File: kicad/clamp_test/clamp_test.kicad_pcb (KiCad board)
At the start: 2 copper layers, 48.3 x 29.2 mm, 22 parts, among them J1 Conn_Coaxial, J2 Conn_Coaxial, J3 Conn_01x03_Pin, U1 LT1365CS, U2 BUF634A

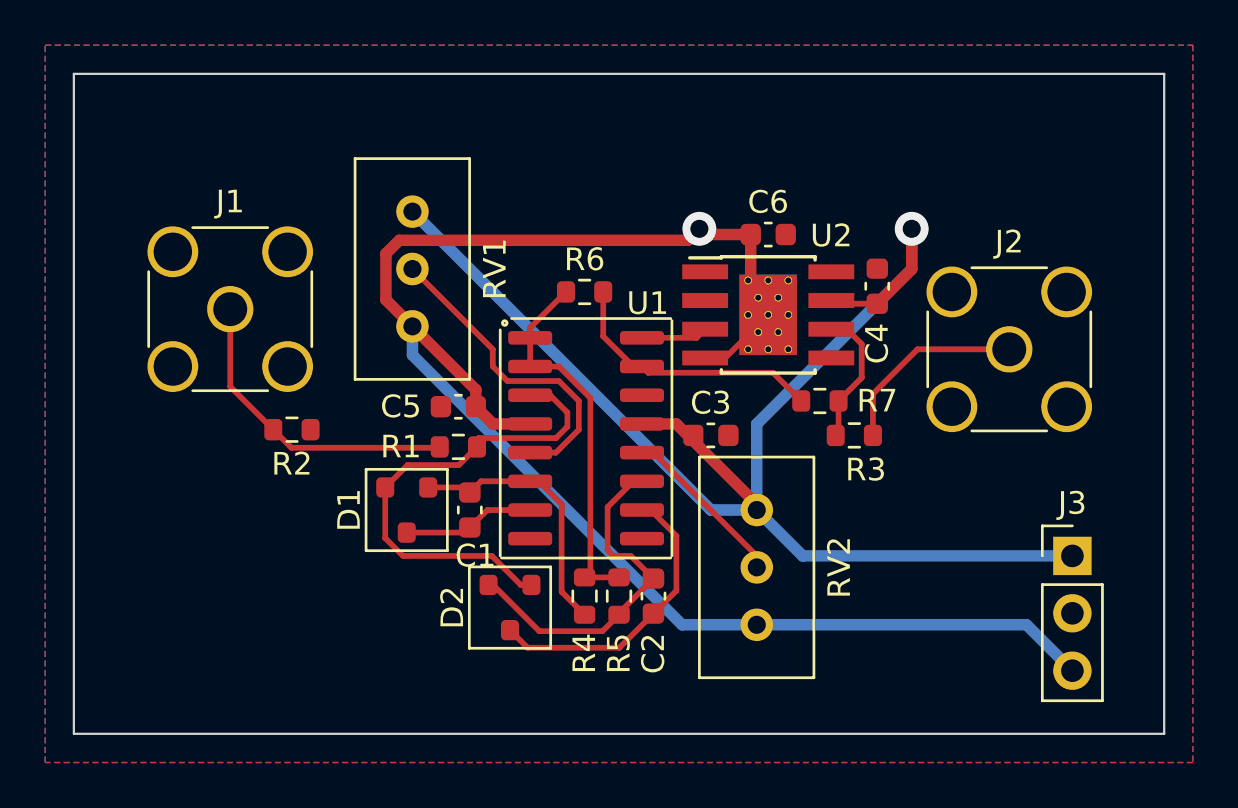
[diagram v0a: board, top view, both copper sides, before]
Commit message: Clamp test board: removed unused vias
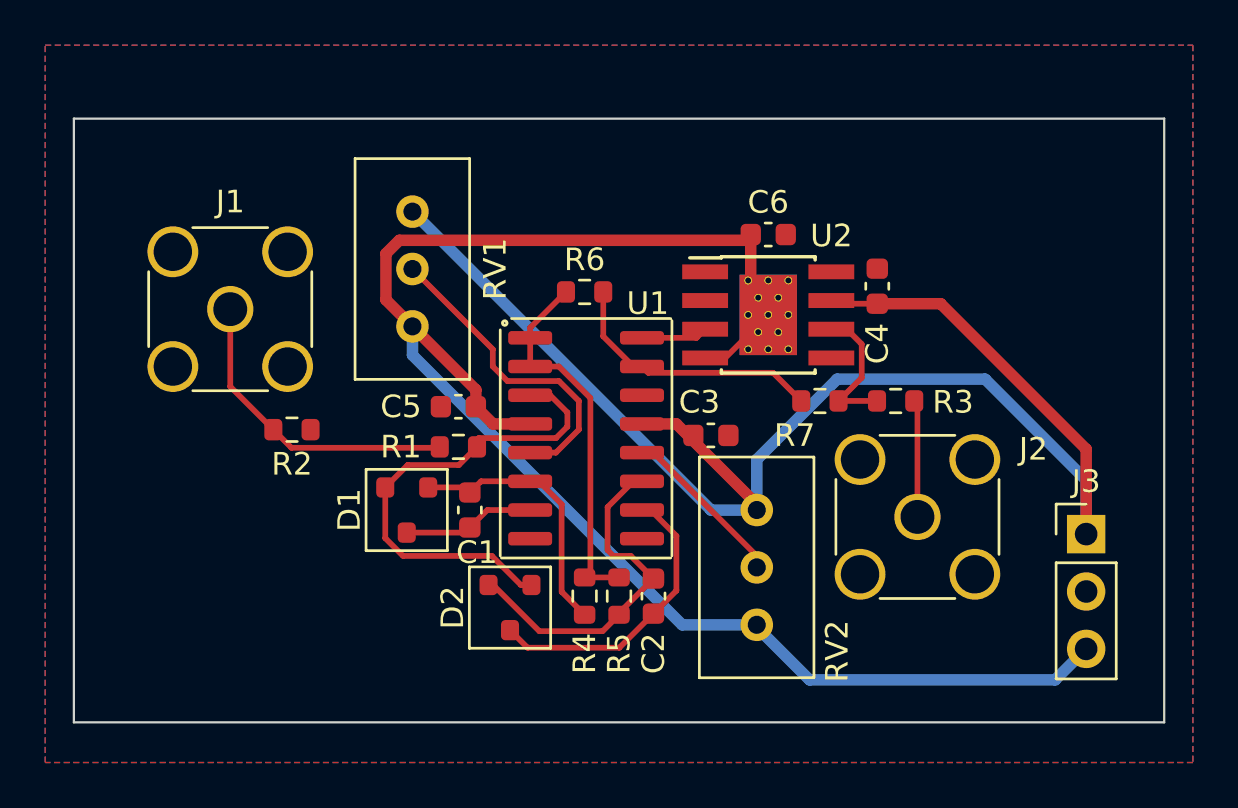
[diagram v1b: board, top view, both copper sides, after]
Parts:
- moved J2 8.46 mm to (51.3, 33.6)
- moved R3 2.38 mm to (50.3, 28.4)
- moved J3 1.14 mm to (58.8, 34.3)
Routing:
- net +12V: track 63.7 -> 67.8 mm, vias 1 -> 0
- net Net-(J2-In): track 8.69 -> 5.19 mm
- net -12V: track 71.6 -> 72.8 mm, vias 1 -> 0
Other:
- board size 48.3 x 29.2 mm -> 48.3 x 26.7 mm

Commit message: Changed buffer position
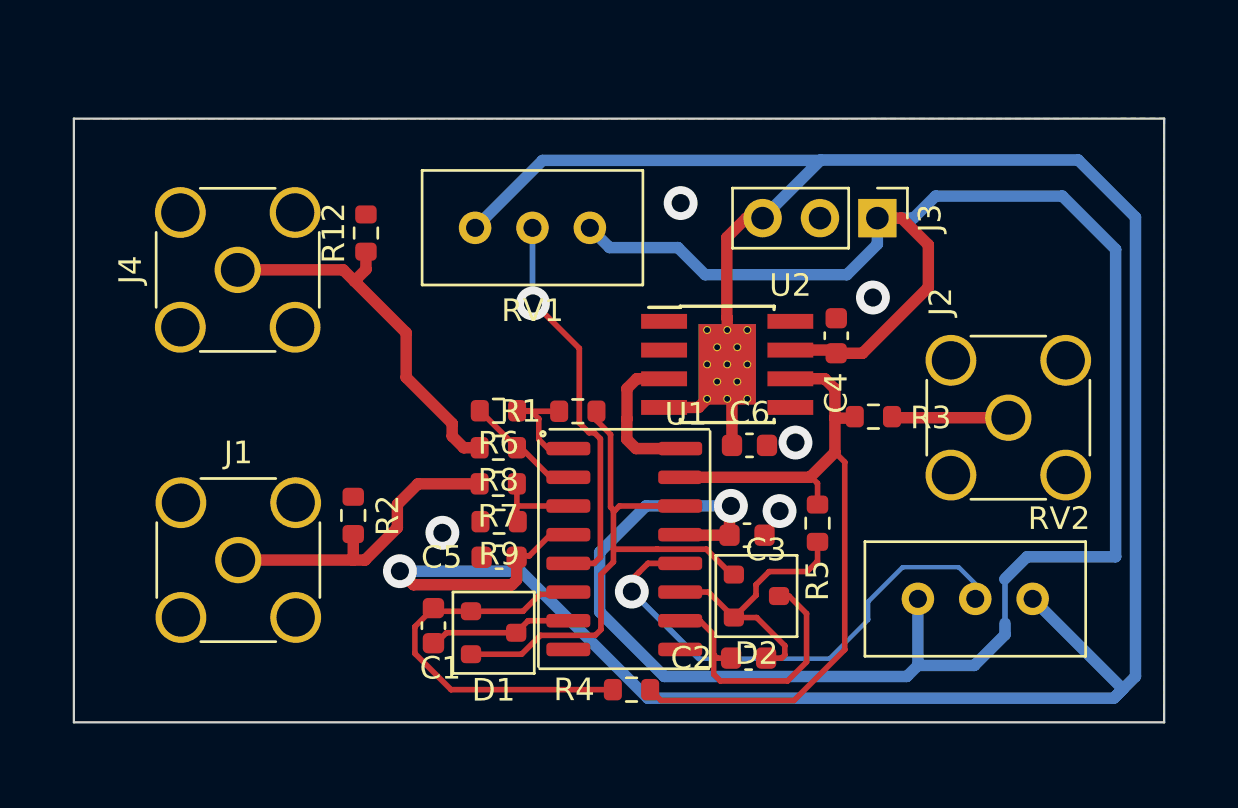
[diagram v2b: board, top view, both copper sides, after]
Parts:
- added J4: Conn_Coaxial, Connector_Coaxial:SMA_Amphenol_132291_Vertical, F.Cu at (21.2, 22.6)
- added R12: 50, Resistor_SMD:R_0603_1608Metric, F.Cu at (26.9, 21.0)
- added R8: 10k, Resistor_SMD:R_0603_1608Metric, F.Cu at (32.8, 30.5)
- added R9: 10k, Resistor_SMD:R_0603_1608Metric, F.Cu at (32.8, 33.8)
- R1: value 10k -> 1k
- moved J3 16.8 mm to (49.5, 20.4), turned to -90 degrees
- moved R7 14.7 mm to (32.8, 32.1), turned to 180 degrees
- moved RV2 12.3 mm to (56.4, 37.2), turned to 0 degrees
- moved J1 11.1 mm to (21.2, 35.5)
- moved D2 10.9 mm to (44.2, 37.1), turned to 0 degrees
- moved C6 9.37 mm to (43.9, 30.4)
- moved R5 9.36 mm to (46.9, 33.9)
- moved C5 6.90 mm to (32.8, 35.4)
- moved D1 6.65 mm to (32.5, 38.7), turned to 0 degrees
- moved R6 6.50 mm to (32.8, 28.9), turned to 180 degrees
- moved J2 5.95 mm to (55.3, 29.2), turned to 90 degrees
- moved R1 5.52 mm to (36.3, 28.9)
- moved C1 5.37 mm to (29.9, 38.4)
- moved U1 5.18 mm to (38.3, 35.0)
- moved RV1 5.17 mm to (31.7, 20.8), turned to 180 degrees
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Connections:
- D1 pad 2: Net-(U1A-+) -> Net-(U1D-+)
- D2 pad 1: Net-(U1A-+) -> Net-(U1D-+)
- R1 pad 1: VIN -> Net-(R1-Pad1)
- R1 pad 2: Net-(U1A-+) -> Net-(U1D-+)
- R4 pad 2: Net-(U1A--) -> VOUT
- R5 pad 2: Net-(U1A--) -> VOUT
- R6 pad 1: Net-(U1A--) -> Net-(R1-Pad1)
- R6 pad 2: Net-(U1D--) -> Net-(U1A--)
- R7 pad 1: Net-(U1D--) -> Net-(U1A-+)
- R7 pad 2: VOUT -> VIN
- U1 pad 1: Net-(U1A--) -> Net-(R1-Pad1)
- U1 pad 14: GND -> Net-(U1D-+)
- U1 pad 15: Net-(U1D--) -> VOUT
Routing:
- net -12V: track 72.8 -> 120.6 mm, vias 0 -> 1
- net +12V: track 67.8 -> 96.3 mm, vias 0 -> 1
- net VOUT: track 6.26 -> 33.2 mm
- net Net-(U1D-+): track 0.00 -> 25.2 mm
- net Net-(U1A-+): track 21.5 -> 3.99 mm
- net ~VIN: track 0.00 -> 17.0 mm
- net VCLAMPP: track 7.48 -> 22.5 mm, vias 0 -> 1
- net Net-(U1D--): track 11.9 -> 0.00 mm
- net Net-(U1A--): track 16.8 -> 5.14 mm
- net Net-(U1B--): track 11.9 -> 18.2 mm
- net Net-(R1-Pad1): track 0.00 -> 5.37 mm
- net Net-(U2-IN): track 2.95 -> 6.61 mm
- net VCLAMPN: track 14.1 -> 17.6 mm, vias 0 -> 1
- net Net-(U1C--): track 15.6 -> 12.8 mm
- net Net-(C2-Pad2): track 13.2 -> 12.6 mm
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
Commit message: adjusted layout
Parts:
- moved C2 7.13 mm to (36.7, 40.0)
- moved R5 5.35 mm to (41.6, 34.9), turned to 0 degrees
- moved R12 3.60 mm to (23.8, 19.2)
- moved R2 2.77 mm to (23.8, 32.4)
- moved J1 2.77 mm to (18.7, 34.3)
- moved J4 2.75 mm to (18.7, 21.5), turned to 0 degrees
- moved C5 2.67 mm to (30.5, 34.0)
- moved R9 2.64 mm to (30.5, 32.5)
- moved R7 2.54 mm to (30.5, 31.0)
- moved R8 2.51 mm to (30.5, 29.5)
- moved R6 2.47 mm to (30.5, 27.9)
- moved C3 2.46 mm to (41.6, 33.1)
- moved C4 2.41 mm to (45.6, 24.4)
- moved R1 2.39 mm to (34.2, 27.7)
- moved R3 2.39 mm to (47.3, 28.0)
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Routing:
- net VOUT: track 33.2 -> 29.8 mm
- net -12V: track 120.6 -> 117.8 mm, vias 1 -> 2
- net ~VIN: track 17.0 -> 19.5 mm
- net Net-(U1D-+): track 25.2 -> 27.8 mm
- net Net-(U1C--): track 12.8 -> 10.4 mm
- net Net-(R1-Pad1): track 5.37 -> 3.73 mm
- net Net-(C2-Pad2): track 12.6 -> 13.9 mm
- net VCLAMPP: track 22.5 -> 23.8 mm
- net +12V: track 96.3 -> 95.0 mm, vias 1 -> 2
- net Net-(U1B--): track 18.2 -> 17.1 mm
- net Net-(C1-Pad2): track 6.38 -> 6.96 mm
- net GND: vias 5 -> 4
